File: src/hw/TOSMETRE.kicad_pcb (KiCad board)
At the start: 2 copper layers, 94 x 50.8 mm, 14 parts, among them J2 Conn_01x01_Female, J3 Conn_01x01, J4 Conn_01x01, U1 16F88_SSOP, U2 L7805, Y1 Crystal

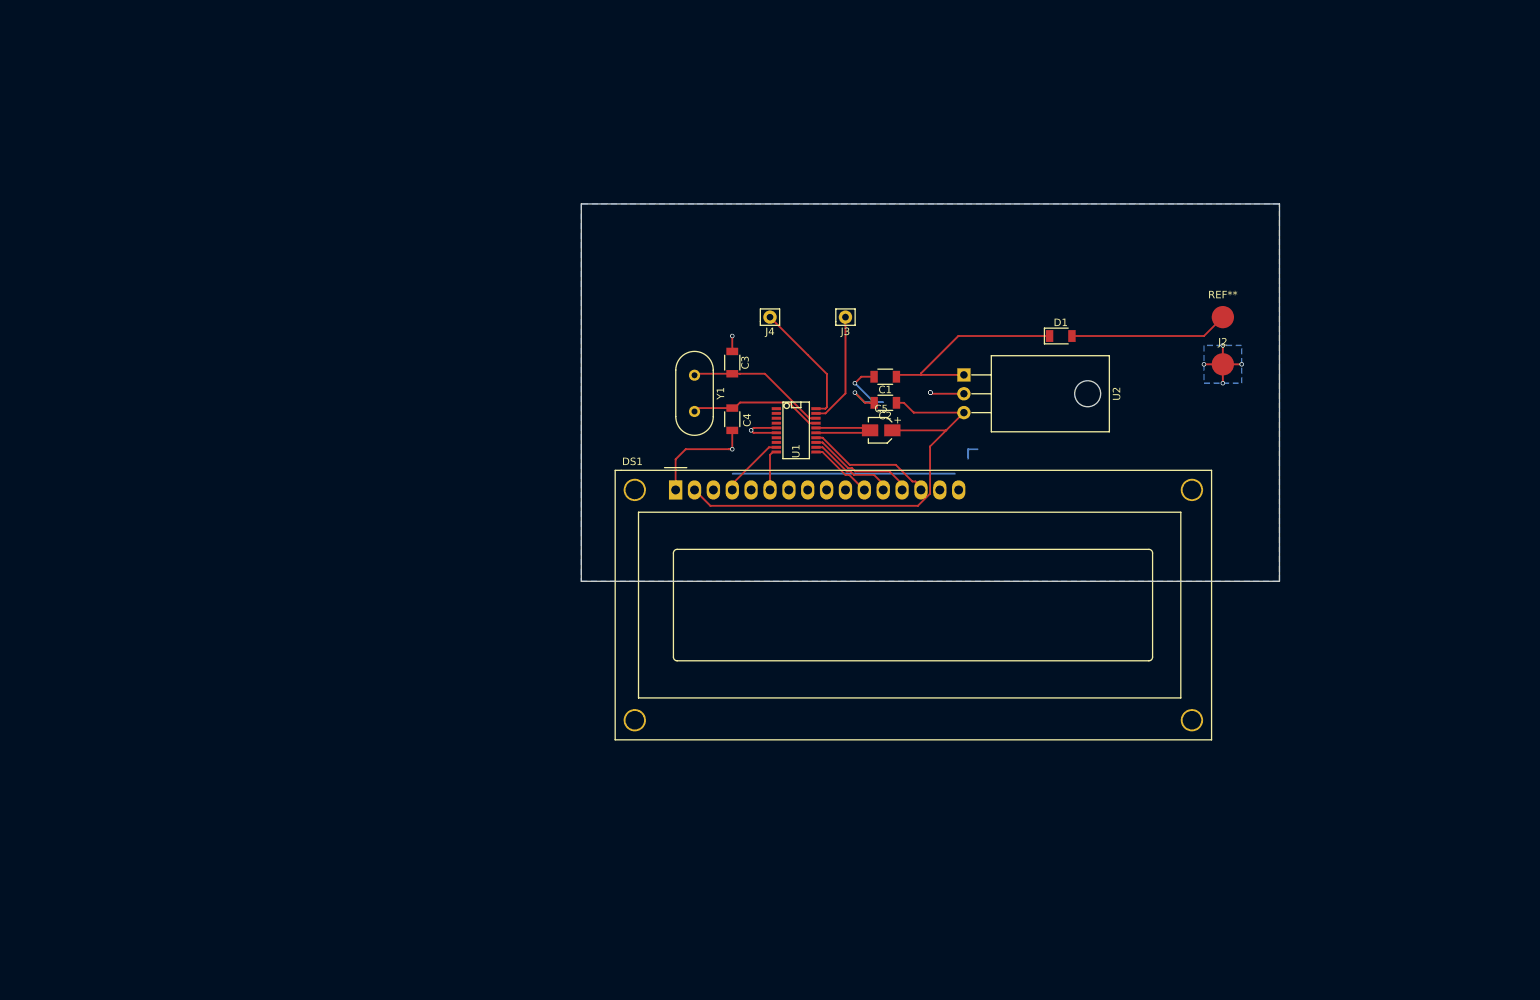
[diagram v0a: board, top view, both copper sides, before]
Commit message: Modification C5 Modification du PCB suite modif c5 Preparation dimension PCB pour ligne 50 Ohms
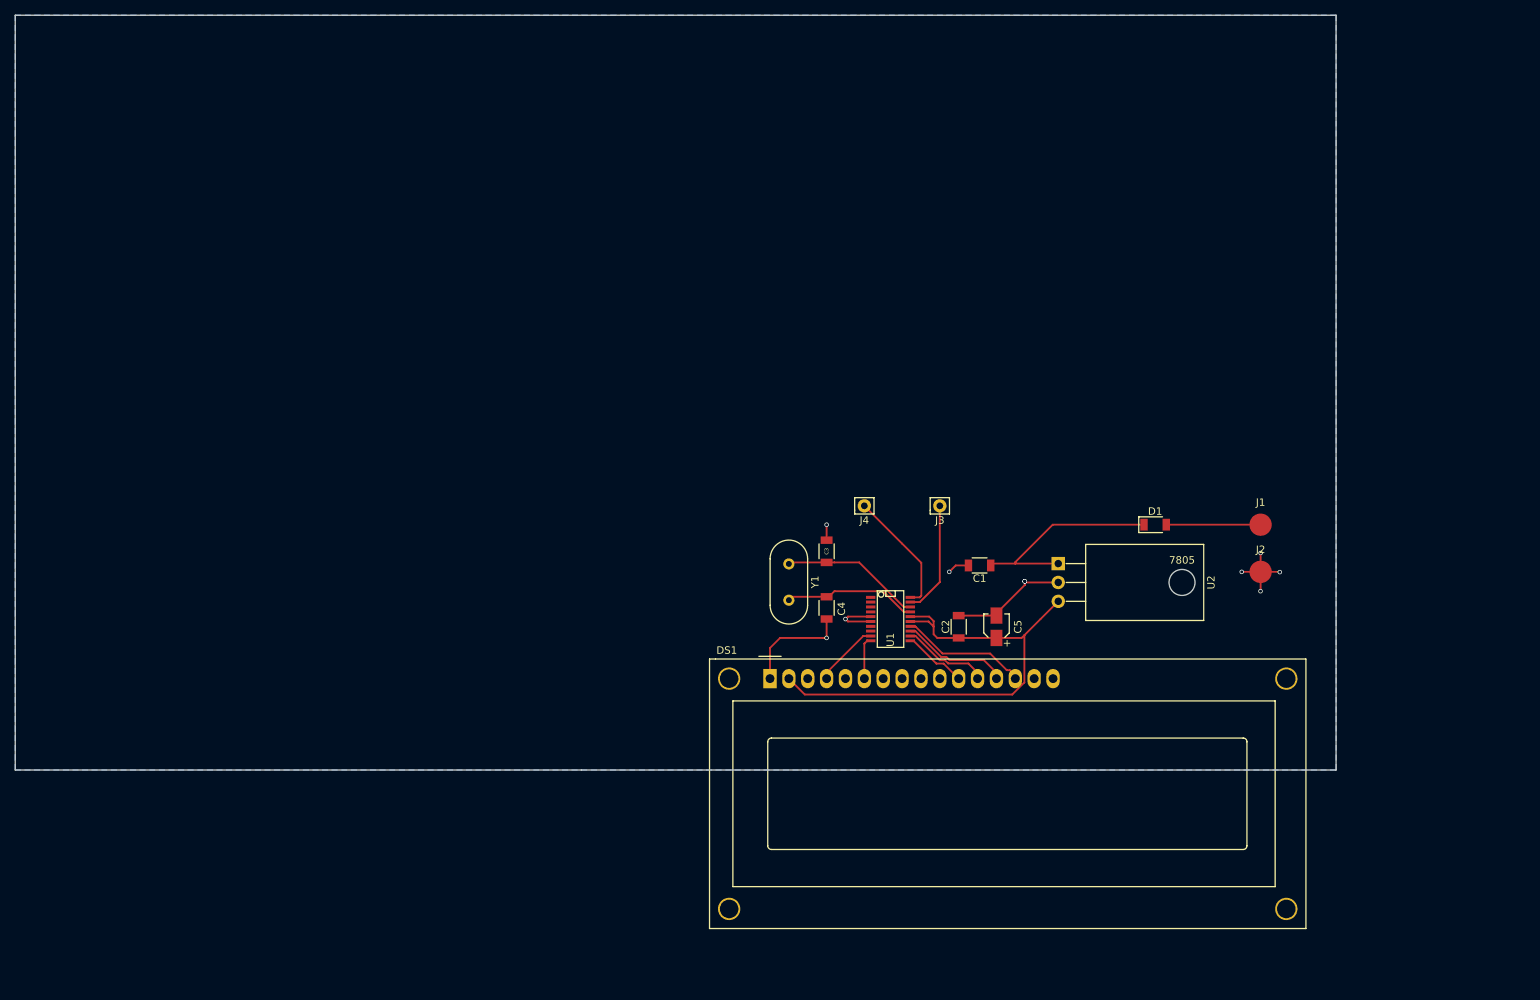
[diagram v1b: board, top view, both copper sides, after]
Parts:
- added J1: +, Measurement_Points:Measurement_Point_Round-SMD-Pad_Big, F.Cu at (226.1, 121.9)
- J2: value Conn_01x01_Female -> -
- moved 7805 36.1 mm to (215.5, 129.7)
- moved C2 31.7 mm to (185.4, 135.7), turned to 90 degrees
- moved C5 30.7 mm to (190.5, 135.7), turned to 90 degrees
- moved J2 28.4 mm to (226.1, 128.3)
- moved D1 28.4 mm to (211.9, 121.9)
- moved C3 28.4 mm to (167.6, 125.5)
- moved C4 28.4 mm to (167.6, 133.1)
- moved DS1 28.4 mm to (160.0, 142.6)
- moved U1 28.4 mm to (176.2, 134.6)
- moved Y1 28.4 mm to (162.6, 127.2)
- moved C1 28.4 mm to (188.2, 127.4)
- moved J3 28.4 mm to (182.9, 119.4)
- moved J4 28.4 mm to (172.7, 119.4)
- moved U2 28.4 mm to (198.8, 127.2)
- renumbered REF** to 7805
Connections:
- C3 pad 1: GNDREF -> Net-(C3-Pad1)
- C5 pad 2: Net-(C5-Pad2) -> GNDREF
- U1 pad 15: Net-(C5-Pad2) -> Net-(C2-Pad1)
- U1 pad 16: Net-(C5-Pad2) -> Net-(C2-Pad1)
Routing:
- net Net-(DS1-Pad16): track 29.9 -> 0.00 mm
- net Net-(C5-Pad2): track 14.8 -> 0.00 mm
- net Net-(D1-Pad2): track 21.4 -> 12.7 mm
- net Net-(C2-Pad1): track 63.6 -> 67.6 mm
- net (no net): track 2.54 -> 0.00 mm
- net GNDREF: track 53.6 -> 51.2 mm, vias 11 -> 9
- net Net-(C3-Pad1): track 0.00 -> 2.08 mm, vias 0 -> 1
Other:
- board size 94 x 50.8 mm -> 177.8 x 101.6 mm

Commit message: oubli du via de masse sur C3
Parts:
- J1: value + -> Conn_01x01_Female
- J2: value - -> Conn_01x01_Female
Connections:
- C3 pad 1: Net-(C3-Pad1) -> GNDREF
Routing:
- net Net-(C3-Pad1): track 2.08 -> 0.00 mm, vias 1 -> 0
- net GNDREF: track 51.2 -> 53.2 mm, vias 9 -> 10
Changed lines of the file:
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@@
 (kicad_pcb (version 4) (host pcbnew 4.0.7)
   (general
-    (links 28)
-    (no_connects 4)
+    (links 29)
+    (no_connects 5)
     (area 58.369999 53.289999 236.270001 154.990001)
     (thickness 1.6)
@@
     (zones 0)
     (modules 15)
-    (nets 30)
+    (nets 29)
   )
   (page A4)
@@
   (net 27 "Net-(DS1-Pad15)")
   (net 28 "Net-(DS1-Pad16)")
-  (net 29 "Net-(C3-Pad1)")
   (net_class Default "Ceci est la Netclass par défaut"
     (clearance 0.2)
@@
     (add_net "Net-(C1-Pad1)")
     (add_net "Net-(C2-Pad1)")
-    (add_net "Net-(C3-Pad1)")
     (add_net "Net-(C3-Pad2)")
     (add_net "Net-(C4-Pad2)")
@@
     (fp_line (start 2.25 1.05) (end -2.25 1.05) (layer F.CrtYd) (width 0.05))
     (pad 1 smd rect (at -1.5 0 270) (size 1 1.6) (layers F.Cu F.Paste F.Mask)
-      (net 29 "Net-(C3-Pad1)"))
+      (net 2 GNDREF))
     (pad 2 smd rect (at 1.5 0 270) (size 1 1.6) (layers F.Cu F.Paste F.Mask)
       (net 4 "Net-(C3-Pad2)"))
@@
       (effects (font (size 1 1) (thickness 0.15)))
     )
-    (fp_text value - (at 4.63 0) (layer F.Fab)
+    (fp_text value Conn_01x01_Female (at 4.63 0) (layer F.Fab)
       (effects (font (size 1 1) (thickness 0.25)))
     )
@@
       (effects (font (size 1 1) (thickness 0.15)))
     )
-    (fp_text value + (at 4.47 -0.04) (layer F.Fab)
+    (fp_text value Conn_01x01_Female (at 4.47 -0.04) (layer F.Fab)
       (effects (font (size 1 1) (thickness 0.15)))
     )
@@
   (segment (start 189.732 127.104) (end 189.732 127.404) (width 0.25) (layer F.Cu) (net 1))
   (segment (start 189.732 127.704) (end 189.732 127.404) (width 0.25) (layer F.Cu) (net 1))
+  (via (at 167.64 121.92) (size 0.6) (drill 0.4) (layers F.Cu B.Cu) (net 2))
+  (segment (start 167.64 124) (end 167.64 121.92) (width 0.25) (layer F.Cu) (net 2))
   (segment (start 190.5 134.16) (end 190.5 133.86) (width 0.25) (layer F.Cu) (net 2))
   (segment (start 190.5 133.86) (end 194.31 130.05) (width 0.25) (layer F.Cu) (net 2))
@@
   (segment (start 180.384538 127.044538) (end 177.8 124.46) (width 0.25) (layer F.Cu) (net 20))
   (segment (start 177.8 124.46) (end 172.72 119.38) (width 0.25) (layer F.Cu) (net 20))
-  (via (at 167.64 121.92) (size 0.6) (drill 0.4) (layers F.Cu B.Cu) (net 29))
-  (segment (start 167.64 124) (end 167.64 121.92) (width 0.25) (layer F.Cu) (net 29))
   (zone (net 2) (net_name GNDREF) (layer B.Cu) (hatch edge 0.508)
     (connect_pads (clearance 0.508))
@@
     (polygon
       (pts
-        (xy 58.42 154.94) (xy 58.42 53.34) (xy 236.22 53.34) (xy 236.22 154.94)
+        (xy 236.22 53.34) (xy 236.22 154.94) (xy 58.42 154.94) (xy 58.42 53.34)
       )
     )

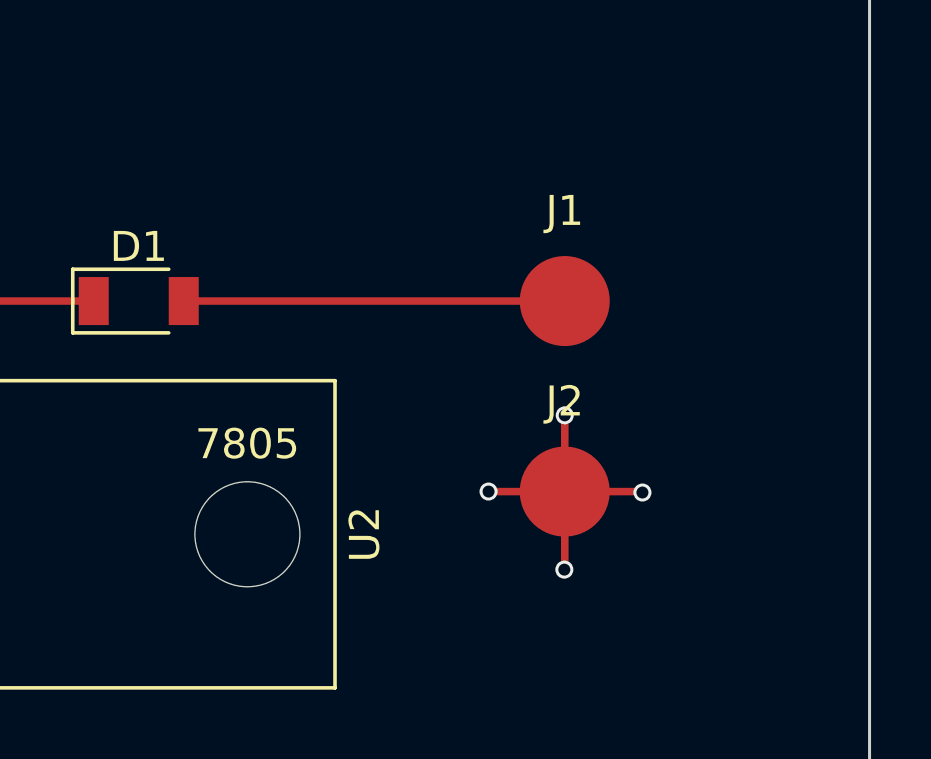
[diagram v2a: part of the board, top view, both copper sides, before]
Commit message: modification alimentation de la platine
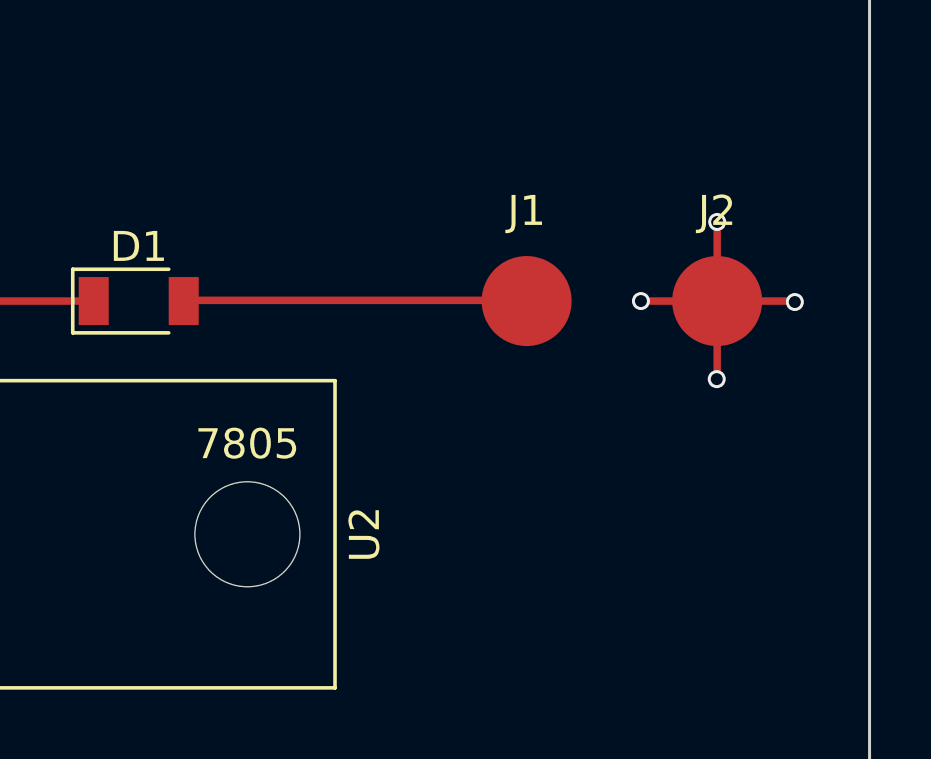
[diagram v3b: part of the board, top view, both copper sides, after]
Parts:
- 7805: value Measurement_Point_Round-SMD-Pad_Big -> (none)
- J1: value Conn_01x01_Female -> +
- J2: value Conn_01x01_Female -> -
- moved J2 8.13 mm to (231.1, 121.9)
- moved J1 1.27 mm to (224.8, 121.9)

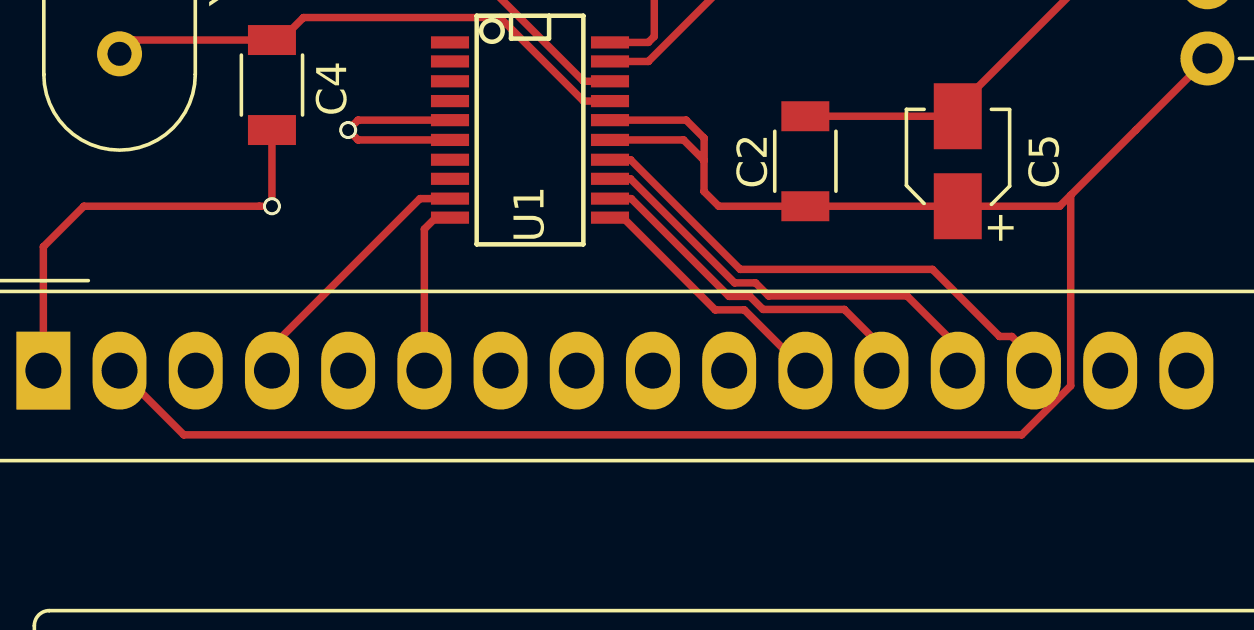
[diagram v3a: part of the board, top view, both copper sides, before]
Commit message: deplacement piste entre borne 14 et 15 du LCD suite a contact
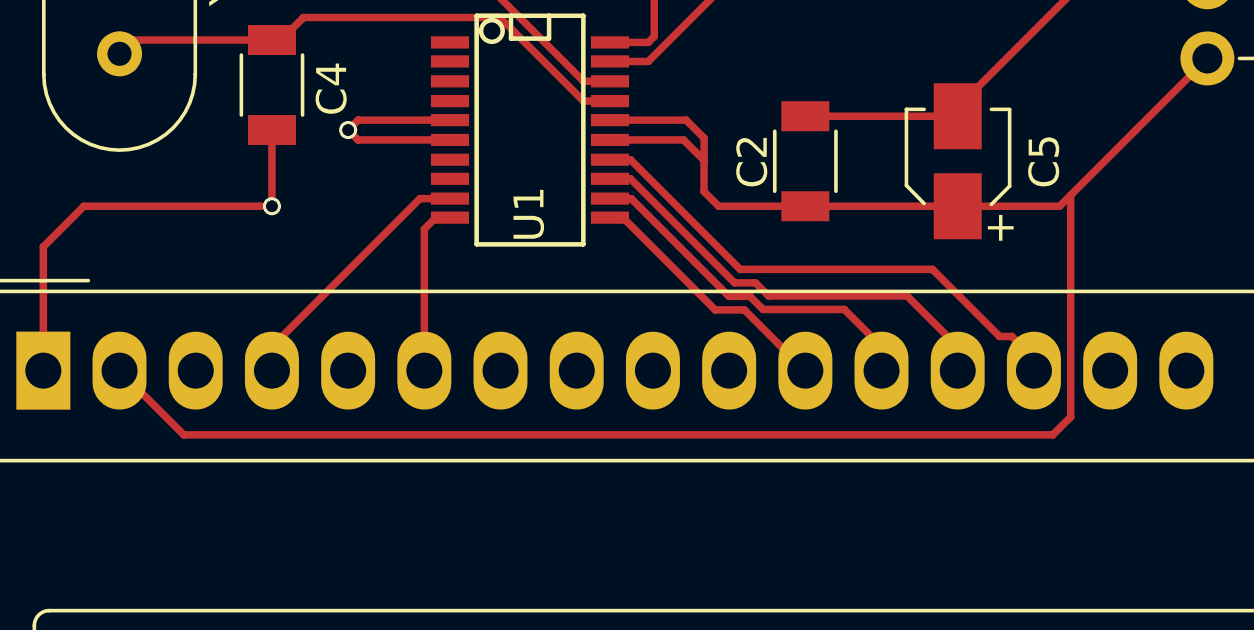
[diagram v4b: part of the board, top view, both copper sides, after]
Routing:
- net Net-(C2-Pad1): track 67.6 -> 68.2 mm
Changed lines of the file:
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@@
 (kicad_pcb (version 4) (host pcbnew 4.0.7)
   (general
-    (links 0)
+    (links 29)
     (no_connects 0)
-    (area 55.92 53.289999 238.485239 178.375)
+    (area 55.92 53.289999 236.270001 178.375)
     (thickness 1.6)
     (drawings 9)
@@
   (via (at 167.64 137.16) (size 0.6) (drill 0.4) (layers F.Cu B.Cu) (net 2))
   (segment (start 167.64 137.16) (end 167.64 134.62) (width 0.25) (layer F.Cu) (net 2))
+  (segment (start 162.56 142.64) (end 164.7 144.78) (width 0.25) (layer F.Cu) (net 3))
+  (segment (start 164.7 144.78) (end 193.670493 144.78) (width 0.25) (layer F.Cu) (net 3))
+  (segment (start 193.670493 144.78) (end 194.26501 144.185483) (width 0.25) (layer F.Cu) (net 3))
+  (segment (start 194.26501 144.185483) (end 194.26501 136.79099) (width 0.25) (layer F.Cu) (net 3))
   (segment (start 178.909 134.9502) (end 181.362264 134.9502) (width 0.25) (layer F.Cu) (net 3))
   (segment (start 182.02851 135.616446) (end 182.02851 135.617371) (width 0.25) (layer F.Cu) (net 3))
@@
   (segment (start 190.5 137.16) (end 185.42 137.16) (width 0.25) (layer F.Cu) (net 3))
   (segment (start 162.56 142.24) (end 162.56 142.64) (width 0.25) (layer F.Cu) (net 3))
-  (segment (start 162.56 142.64) (end 164.7 144.78) (width 0.25) (layer F.Cu) (net 3))
-  (segment (start 164.7 144.78) (end 192.632425 144.78) (width 0.25) (layer F.Cu) (net 3))
-  (segment (start 192.632425 144.78) (end 194.26501 143.147415) (width 0.25) (layer F.Cu) (net 3))
-  (segment (start 194.26501 143.147415) (end 194.26501 136.79099) (width 0.25) (layer F.Cu) (net 3))
   (segment (start 194.26501 136.79099) (end 196.436 134.62) (width 0.25) (layer F.Cu) (net 3))
   (segment (start 196.436 134.62) (end 198.822 132.234) (width 0.25) (layer F.Cu) (net 3))
